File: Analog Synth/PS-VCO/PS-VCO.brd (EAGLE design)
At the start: 50 x 50 mm, 44 parts, among them IC1 TL084D, Q1 BC847BS, Q2 2N3906, T1 2N3904, T2 2N3904

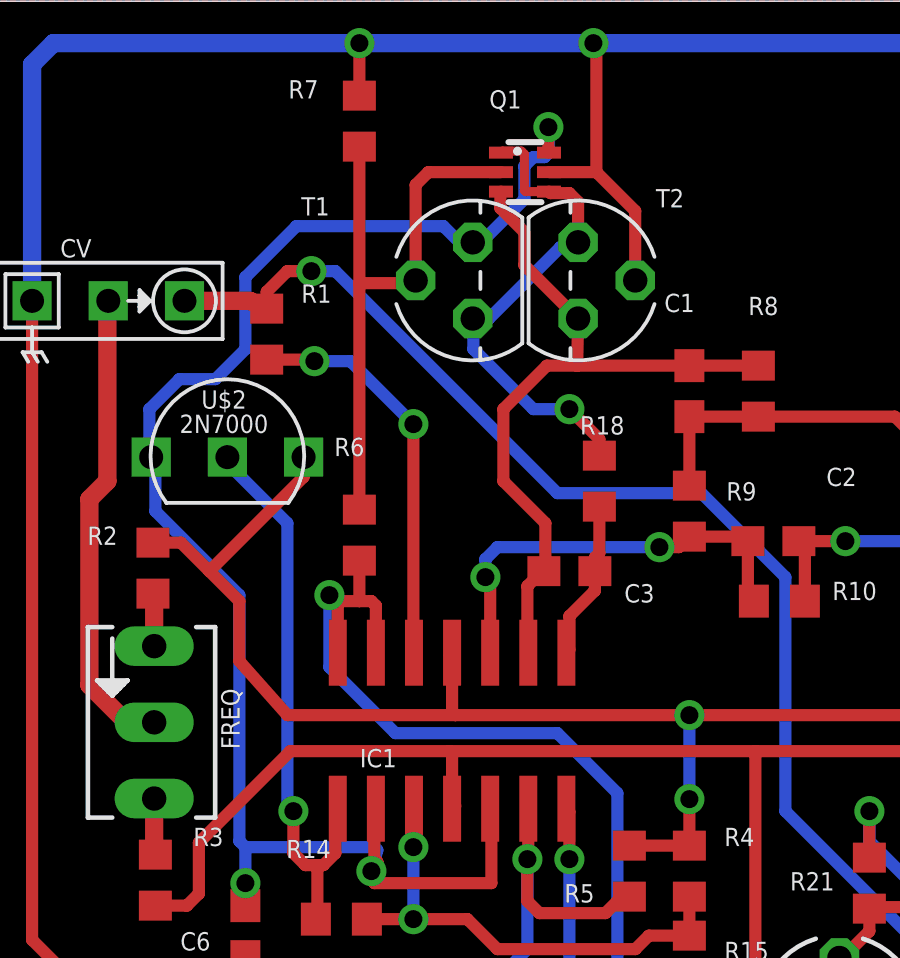
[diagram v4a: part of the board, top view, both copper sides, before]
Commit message: PS-VCO: updating documentation and schematic. rendered pdfs for schematic and pcb. generated a BOM
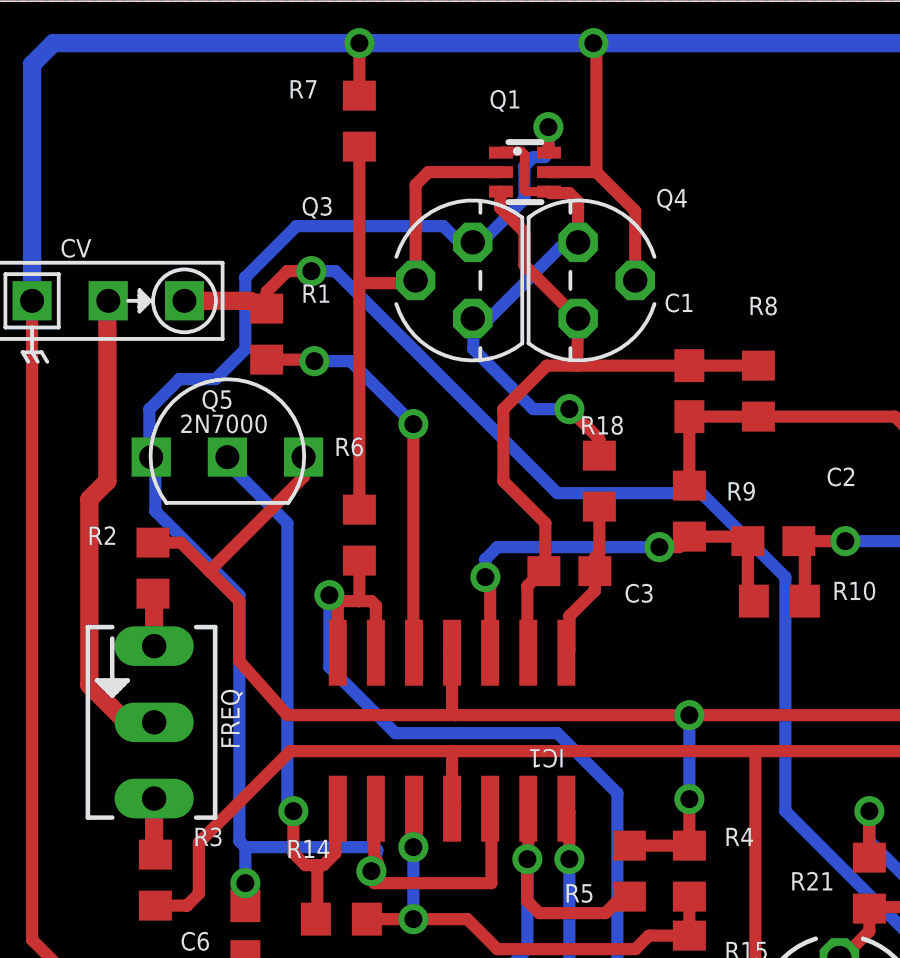
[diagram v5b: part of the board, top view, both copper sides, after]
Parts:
- C1, C2, C5: value 0.1u -> 100n
- CV: value I/O -> CV
- renumbered T1 to Q3, T2 to Q4, U$2 to Q5
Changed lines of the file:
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@@
 <grid distance="0.1" unitdist="inch" unit="inch" style="lines" multiple="1" display="no" altdistance="0.01" altunitdist="inch" altunit="inch"/>
 <layers>
-<layer number="1" name="Top" color="4" fill="1" visible="yes" active="yes"/>
+<layer number="1" name="Top" color="4" fill="1" visible="no" active="yes"/>
 <layer number="2" name="Route2" color="1" fill="3" visible="no" active="no"/>
 <layer number="3" name="Route3" color="4" fill="3" visible="no" active="no"/>
@@
 <layer number="14" name="Route14" color="1" fill="6" visible="no" active="no"/>
 <layer number="15" name="Route15" color="4" fill="6" visible="no" active="no"/>
-<layer number="16" name="Bottom" color="1" fill="1" visible="yes" active="yes"/>
+<layer number="16" name="Bottom" color="1" fill="1" visible="no" active="yes"/>
 <layer number="17" name="Pads" color="2" fill="1" visible="yes" active="yes"/>
 <layer number="18" name="Vias" color="2" fill="1" visible="yes" active="yes"/>
-<layer number="19" name="Unrouted" color="6" fill="1" visible="yes" active="yes"/>
+<layer number="19" name="Unrouted" color="6" fill="1" visible="no" active="yes"/>
 <layer number="20" name="Dimension" color="15" fill="1" visible="yes" active="yes"/>
 <layer number="21" name="tPlace" color="7" fill="1" visible="yes" active="yes"/>
@@
 <text x="43.6" y="18.2" size="1.016" layer="27" rot="R180">GND</text>
 <text x="43.6" y="15.6" size="1.016" layer="27" rot="R180">-12</text>
-<text x="43.6" y="13" size="1.016" layer="27" rot="R180">CV_IN</text>
-<text x="43.6" y="10.6" size="1.016" layer="27" rot="R180">SQUARE</text>
+<text x="43.6" y="10.46" size="1.016" layer="27" rot="R180">CV_IN</text>
+<text x="43.6" y="13.14" size="1.016" layer="27" rot="R180">SQUARE</text>
 <text x="27.908" y="3.728" size="3.81" layer="27">PS-VCO</text>
 <text x="35.474" y="1.664" size="1.27" layer="27">Ryan Jensen</text>
@@
 <elements>
 <element name="IC1" library="linear" package="SO14" value="TL084D" x="19.09" y="25.68" smashed="yes" rot="R180">
-<attribute name="NAME" x="16.015" y="24.462" size="0.6096" layer="25"/>
-<attribute name="VALUE" x="15.815" y="25.248" size="1.016" layer="27"/>
-</element>
-<element name="CV" library="!synth_sch" package="MONO_JACK" value="I/O" x="7.63" y="40.01" smashed="yes">
+<attribute name="NAME" x="22.847" y="25.068" size="0.6096" layer="25" rot="SR180"/>
+<attribute name="VALUE" x="23.047" y="26.568" size="1.016" layer="27" rot="SR180"/>
+</element>
+<element name="CV" library="!synth_sch" package="MONO_JACK" value="CV" x="7.63" y="40.01" smashed="yes">
 <attribute name="NAME" x="6.0298" y="41.4578" size="0.6096" layer="25"/>
 </element>
@@
 <attribute name="VALUE" x="21.4" y="46.18" size="0.6096" layer="27" rot="R180"/>
 </element>
-<element name="T1" library="transistor" package="TO92" value="2N3904" x="19.78" y="40.69" smashed="yes" rot="R90">
+<element name="Q3" library="transistor" package="TO92" value="2N3904" x="19.78" y="40.69" smashed="yes" rot="R90">
 <attribute name="NAME" x="14.065" y="42.855" size="0.6096" layer="25" ratio="10"/>
 <attribute name="VALUE" x="14.065" y="41.95" size="0.6096" layer="27" ratio="10"/>
 </element>
-<element name="T2" library="transistor" package="TO92" value="2N3904" x="23.29" y="40.69" smashed="yes" rot="R270">
+<element name="Q4" library="transistor" package="TO92" value="2N3904" x="23.29" y="40.69" smashed="yes" rot="R270">
 <attribute name="NAME" x="25.885" y="43.125" size="0.6096" layer="25" ratio="10"/>
 <attribute name="VALUE" x="25.885" y="42.22" size="0.6096" layer="27" ratio="10"/>
@@
 <attribute name="VALUE" x="14.635" y="46.505" size="0.6096" layer="27" rot="R180"/>
 </element>
-<element name="C1" library="rcl" package="C0603" value="0.1u" x="27" y="37" smashed="yes" rot="R90">
+<element name="C1" library="rcl" package="C0603" value="100n" x="27" y="37" smashed="yes" rot="R90">
 <attribute name="NAME" x="26.165" y="39.635" size="0.6096" layer="25"/>
 <attribute name="VALUE" x="26.165" y="38.695" size="0.6096" layer="27"/>
@@
 <attribute name="VALUE" x="28.965" y="38.595" size="0.6096" layer="27"/>
 </element>
-<element name="C2" library="rcl" package="C0603" value="0.1u" x="29.8" y="32" smashed="yes">
+<element name="C2" library="rcl" package="C0603" value="100n" x="29.8" y="32" smashed="yes">
 <attribute name="NAME" x="31.565" y="33.835" size="0.6096" layer="25"/>
 <attribute name="VALUE" x="31.565" y="32.895" size="0.6096" layer="27"/>
@@
 <attribute name="VALUE" x="42.555" y="21.35" size="1.27" layer="27" rot="R270"/>
 </element>
-<element name="U$2" library="!synth_sch" package="2N7000" value="2N7000" x="11.6" y="34.8" smashed="yes">
+<element name="Q5" library="!synth_sch" package="2N7000" value="2N7000" x="11.6" y="34.8" smashed="yes">
 <attribute name="NAME" x="10.73" y="36.416" size="0.6096" layer="21"/>
 <attribute name="VALUE" x="10.006" y="35.606" size="0.6096" layer="21"/>
@@
 <attribute name="VALUE" x="28.165" y="20.895" size="0.6096" layer="27"/>
 </element>
-<element name="C5" library="rcl" package="C0603" value="0.1u" x="16.8" y="17.2" smashed="yes" rot="R180">
+<element name="C5" library="rcl" package="C0603" value="100n" x="16.8" y="17.2" smashed="yes" rot="R180">
 <attribute name="NAME" x="15.235" y="17.765" size="0.6096" layer="25" rot="R180"/>
 <attribute name="VALUE" x="15.235" y="16.905" size="0.6096" layer="27" rot="R180"/>
@@
 <signal name="CURRENT_SINK">
 <contactref element="Q1" pad="6"/>
-<contactref element="T1" pad="1"/>
+<contactref element="Q3" pad="1"/>
 <contactref element="IC1" pad="9"/>
 <contactref element="C6" pad="1"/>
-<contactref element="U$2" pad="S"/>
+<contactref element="Q5" pad="S"/>
 <contactref element="IC1" pad="12"/>
 <wire x1="19.78" y1="41.96" x2="20.06" y2="41.96" width="0.4064" layer="16"/>
@@
 <signal name="N$3">
 <contactref element="Q1" pad="1"/>
-<contactref element="T1" pad="3"/>
+<contactref element="Q3" pad="3"/>
 <contactref element="Q1" pad="4"/>
-<contactref element="T2" pad="3"/>
+<contactref element="Q4" pad="3"/>
 <contactref element="R18" pad="2"/>
 <wire x1="23.29" y1="41.96" x2="23.29" y2="43.31" width="0.4064" layer="1"/>
@@
 <signal name="N$4">
 <contactref element="Q1" pad="2"/>
-<contactref element="T1" pad="2"/>
+<contactref element="Q3" pad="2"/>
 <contactref element="R6" pad="2"/>
 <contactref element="R7" pad="2"/>
@@
 <contactref element="R7" pad="1"/>
 <contactref element="Q1" pad="5"/>
-<contactref element="T2" pad="2"/>
+<contactref element="Q4" pad="2"/>
 <contactref element="R10" pad="1"/>
 <contactref element="C2" pad="2"/>
@@
 <contactref element="R5" pad="2"/>
 <contactref element="R4" pad="2"/>
-<contactref element="U$2" pad="D"/>
+<contactref element="Q5" pad="D"/>
 <contactref element="C4" pad="+"/>
 <contactref element="C8" pad="1"/>
@@
 <contactref element="C1" pad="2"/>
 <contactref element="Q1" pad="3"/>
-<contactref element="T2" pad="1"/>
+<contactref element="Q4" pad="1"/>
 <contactref element="C3" pad="2"/>
 <contactref element="IC1" pad="2"/>
@@
 <contactref element="R14" pad="2"/>
 <contactref element="IC1" pad="8"/>
-<contactref element="U$2" pad="G"/>
+<contactref element="Q5" pad="G"/>
 <wire x1="11.6" y1="34.8" x2="11.6" y2="34.6" width="0.4064" layer="16"/>
 <wire x1="11.6" y1="34.6" x2="13.6" y2="32.6" width="0.4064" layer="16"/>

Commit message: updating PS-VCO. Changed a resistor value to get closer to 50% duty cycle. It is still very approximate, but before the duty cycle was around 25% or 30% or something really obviously not balanced.
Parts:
- R5: value 100k -> 120k
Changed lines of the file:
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@@
 <attribute name="VALUE" x="15.235" y="16.905" size="0.6096" layer="27" rot="R180"/>
 </element>
-<element name="R5" library="rcl" package="R0603" value="100k" x="25" y="21" smashed="yes" rot="R90">
+<element name="R5" library="rcl" package="R0603" value="120k" x="25" y="21" smashed="yes" rot="R90">
 <attribute name="NAME" x="23.835" y="20.565" size="0.6096" layer="25" rot="R180"/>
 <attribute name="VALUE" x="23.835" y="19.705" size="0.6096" layer="27" rot="R180"/>
